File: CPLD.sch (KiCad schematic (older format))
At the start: 33 parts, among them J3 JTAG, SW2 User PB, SW3 User DIP, U2 74LVC1G04, U3 EPM7064STC100, X1 CFPS-72 50mhz

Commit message: Renamed to SMC-80
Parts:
- D1, D2, D3, D4, D5, D6, D7, D8, D9: symbol THS-80-rescue:LED-Device-max_breakout-rescue-sbc_z80-rescue -> SMC-80-rescue:LED-Device-max_breakout-rescue-sbc_z80-rescue
- J3: symbol THS-80:Altera-JTAG-10 -> SMC-80:Altera-JTAG-10
- U3: symbol THS-80:EPM7064STC100 -> SMC-80:EPM7064STC100
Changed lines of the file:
@@
 encoding utf-8
 Sheet 2 6
-Title "THS-80"
+Title "SMC-80"
 Date "2019-08-15"
 Rev "1.0"
@@
 TCK
 $Comp
-L THS-80-rescue:LED-Device-max_breakout-rescue-sbc_z80-rescue D?
+L SMC-80-rescue:LED-Device-max_breakout-rescue-sbc_z80-rescue D?
 U 1 1 5DC12F86
 P 5400 6150
@@
 	4900 1950 5050 1950
 $Comp
-L THS-80-rescue:LED-Device-max_breakout-rescue-sbc_z80-rescue D?
+L SMC-80-rescue:LED-Device-max_breakout-rescue-sbc_z80-rescue D?
 U 1 1 5DDEBBC2
 P 5200 2050
@@
 $EndComp
 $Comp
-L THS-80-rescue:LED-Device-max_breakout-rescue-sbc_z80-rescue D?
+L SMC-80-rescue:LED-Device-max_breakout-rescue-sbc_z80-rescue D?
 U 1 1 5DDEBB56
 P 5200 1550
@@
 $EndComp
 $Comp
-L THS-80-rescue:LED-Device-max_breakout-rescue-sbc_z80-rescue D?
+L SMC-80-rescue:LED-Device-max_breakout-rescue-sbc_z80-rescue D?
 U 1 1 5DDEBB50
 P 5200 1750
@@
 $EndComp
 $Comp
-L THS-80-rescue:LED-Device-max_breakout-rescue-sbc_z80-rescue D?
+L SMC-80-rescue:LED-Device-max_breakout-rescue-sbc_z80-rescue D?
 U 1 1 5DDEBB4A
 P 5200 1650
@@
 $EndComp
 $Comp
-L THS-80-rescue:LED-Device-max_breakout-rescue-sbc_z80-rescue D?
+L SMC-80-rescue:LED-Device-max_breakout-rescue-sbc_z80-rescue D?
 U 1 1 5DDEBB44
 P 5200 1950
@@
 $EndComp
 $Comp
-L THS-80-rescue:LED-Device-max_breakout-rescue-sbc_z80-rescue D?
+L SMC-80-rescue:LED-Device-max_breakout-rescue-sbc_z80-rescue D?
 U 1 1 5DDEBB3E
 P 5200 1850
@@
 $EndComp
 $Comp
-L THS-80-rescue:LED-Device-max_breakout-rescue-sbc_z80-rescue D?
+L SMC-80-rescue:LED-Device-max_breakout-rescue-sbc_z80-rescue D?
 U 1 1 5DDEBB22
 P 5200 2150
@@
 $EndComp
 $Comp
-L THS-80-rescue:LED-Device-max_breakout-rescue-sbc_z80-rescue D?
+L SMC-80-rescue:LED-Device-max_breakout-rescue-sbc_z80-rescue D?
 U 1 1 5DDEBB1C
 P 5200 1450
@@
 Connection ~ 8000 950
 $Comp
-L THS-80:EPM7064STC100 U?
+L SMC-80:EPM7064STC100 U?
 U 1 1 5D91E95F
 P 7850 3200
@@
 	8950 3750 9550 3750
 $Comp
-L THS-80:Altera-JTAG-10 J?
+L SMC-80:Altera-JTAG-10 J?
 U 1 1 5DC12FA5
 P 3300 5500

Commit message: trace routing
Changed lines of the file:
@@
 Text Label 9250 2050 0    50   ~ 0
 A7
+Text Label 6300 1350 0    50   ~ 0
+SW0
+Text Label 6300 1250 0    50   ~ 0
+SW1
+Text Label 6350 4250 0    50   ~ 0
+SW2
 Text Label 6350 4150 0    50   ~ 0
-SW0
-Text Label 6350 4250 0    50   ~ 0
-SW1
-Text Label 6350 1250 0    50   ~ 0
-SW2
-Text Label 6350 1350 0    50   ~ 0
 SW3
 Text Label 6300 3350 0    50   ~ 0

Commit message: Routing finished
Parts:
- added C11, C15, C2, C5: 100nF, Capacitor_SMD:C_0603_1608Metric_Pad1.05x0.95mm_HandSolder, symbol Device:C_Small
- added J3: PMOD, Connector_PinSocket_2.54mm:PinSocket_2x06_P2.54mm_Horizontal_Top_Bottom, symbol Connector_Generic:Conn_02x06_Top_Bottom
- added R3: 1K, Resistor_SMD:R_0603_1608Metric_Pad1.05x0.95mm_HandSolder, symbol Device:R_Small
- added RN3: 200R, Resistor_SMD:R_Cat16-8, symbol Device:R_Pack08
- added U1: TXS0108EPW, Package_SO:TSSOP-20_4.4x6.5mm_P0.65mm, symbol Logic_LevelTranslator:TXS0108EPW
- renumbered C7 to C10, C9 to C12, C10 to C13, C11 to C14, C12 to C16, C4 to C3, C2 to C4, C3 to C6, C5 to C7, C6 to C8, C8 to C9, J3 to J4, R2 to R1, R3 to R2, RN3 to RN4, SW3 to SW1
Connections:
- net labels added: +3V3, P1, P10, P2, P3, P4, P7, P8, P9
- wire segments 168 -> 211
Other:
- moved on the sheet: C10, C12, C13, C14, C16, C3, C4, C6, C7, C8, C9, D1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

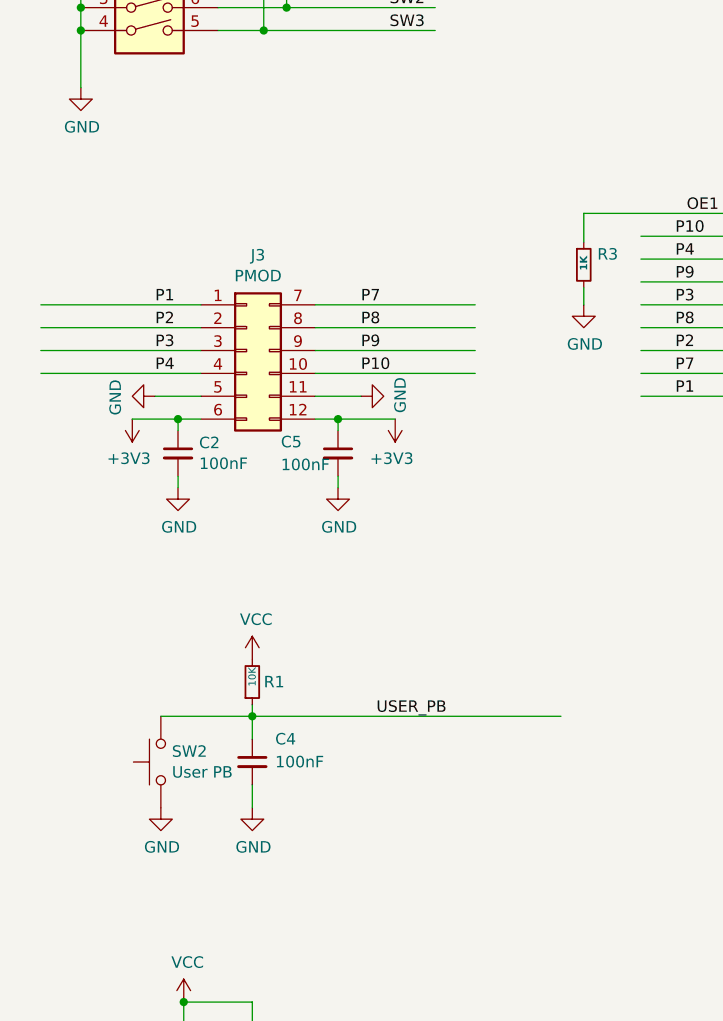
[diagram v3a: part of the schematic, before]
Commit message: reorganized sheets, added SIO clk select
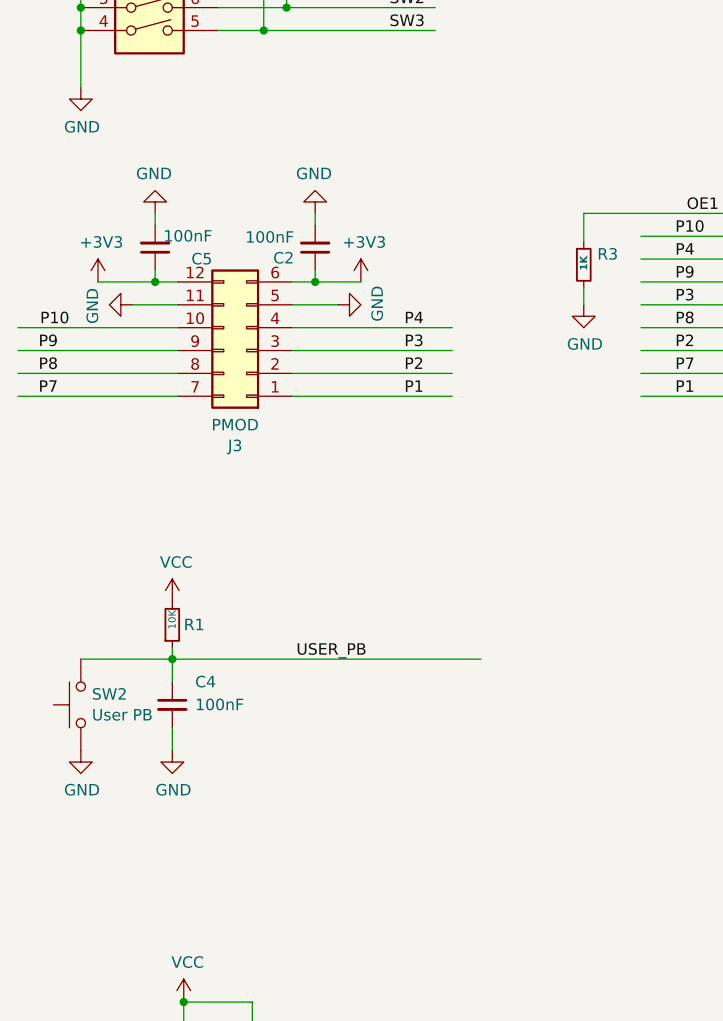
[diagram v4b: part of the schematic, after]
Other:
- moved on the sheet: C2, C4, C5, J3, R1, SW2

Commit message: remove old files, added jtag pullup
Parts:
- added R7: 10K, Resistor_SMD:R_0603_1608Metric_Pad1.05x0.95mm_HandSolder, symbol Device:R_Small
- renumbered C5 to C2, C4 to C3, C3 to C4, C2 to C5, R1 to R2, R2 to R3, R3 to R4, R4 to R5, R5 to R6, R6 to R8, SW1 to SW3, U1 to U2, U2 to U3, U3 to U4
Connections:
- net labels added: PMOD_ENA
- net labels removed: OE1
- wire segments 211 -> 216
